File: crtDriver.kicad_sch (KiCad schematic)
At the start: 72 parts, among them J1 Lum_In, J2 H_Sync, J3 V_Sync, Q1 2N7000, Q10 2N7000, Q11 2N7000, Q12 2N7000, Q13 2N7000, Q14 2N7000, Q15 2N7000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

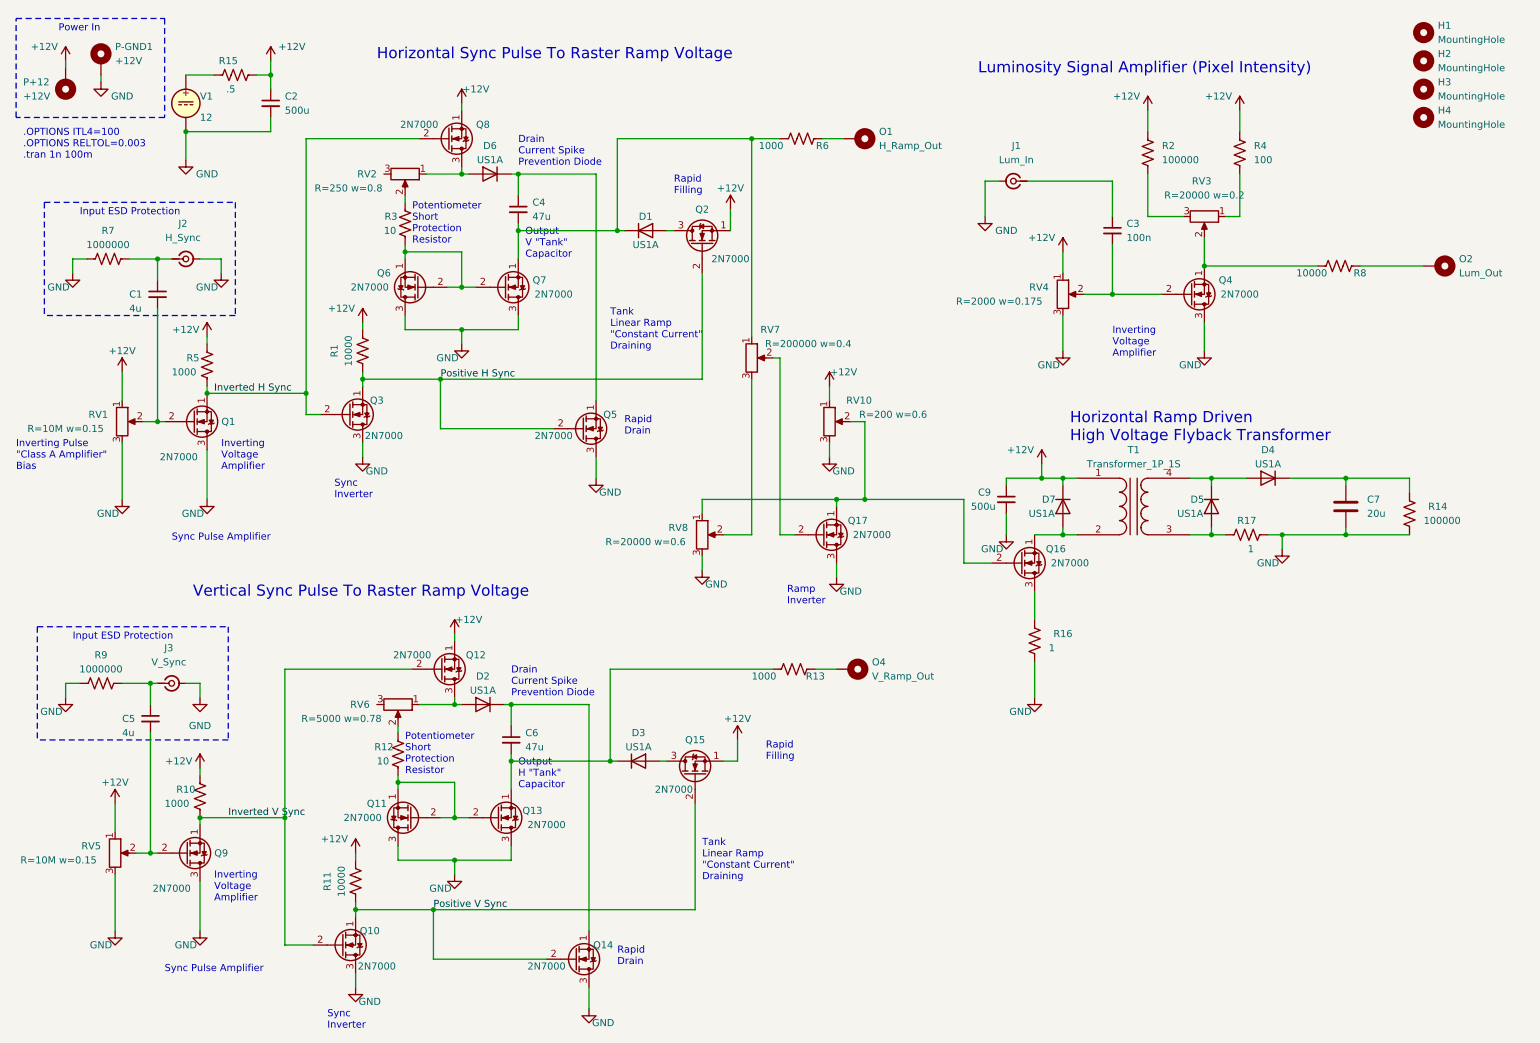
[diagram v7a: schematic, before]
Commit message: updated to kicad 8, simulation for flyback runs though uses 10gb ram or so for 20ms of simulation with 0.01e-03 seconds ish timestep
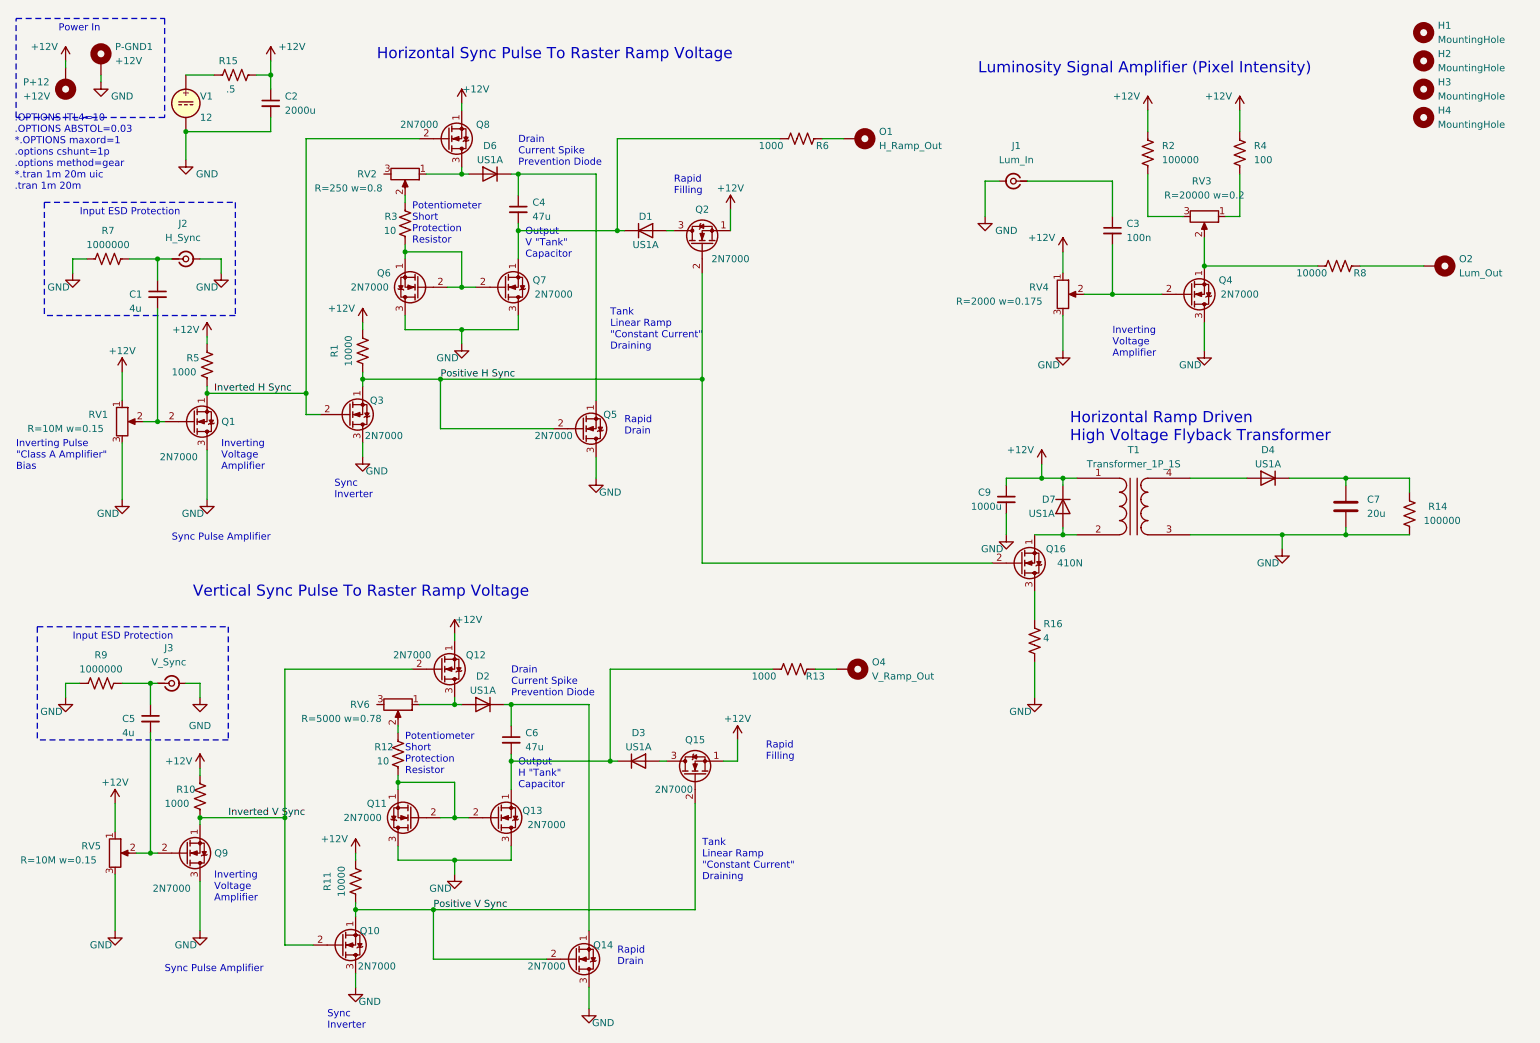
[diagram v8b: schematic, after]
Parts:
- removed D5: US1A, Diode_SMD:D_SMA, symbol Diode:US1A
- removed Q17: 2N7000, Package_TO_SOT_SMD:SOT-23, symbol Transistor_FET:2N7000
- removed R17: 1, Resistor_SMD:R_0603_1608Metric, symbol Device:R_US
- removed RV10, RV7, RV8: 2000, Potentiometer_SMD:Potentiometer_Bourns_TC33X_Vertical, symbol Device:R_Potentiometer
- C2: value 500u -> 2000u
- C9: value 500u -> 1000u
- Q16: value 2N7000 -> 410N
- R16: value 1 -> 4
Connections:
- net GND: now also T1.3 (SA)
- net Positive H Sync: now also Q16.2 (G)
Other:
- note added: ".OPTIONS ITL4=10 .OPTIONS ABSTOL=0.03 *.OPTIONS maxord=1 .options cshunt=1p .options method=gear *.tran 1m 20m uic .tran 1m 20m"
- note removed: ".OPTIONS ITL4=100 .OPTIONS RELTOL=0.003 .tran 1n 100m"
- note removed: "Ramp Inverter"
